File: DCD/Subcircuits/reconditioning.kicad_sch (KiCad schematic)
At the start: 14 parts, among them IC1 830S21AMI-01LF, IC2 830S21AMI-01LF, U15 MC100EP31DTG, U16 MC100EP31DTG, U7 LP2985-33DBVR, U8 CDCLVC1104PWR, Y1 SiT8208AI-21-33E-50.000000

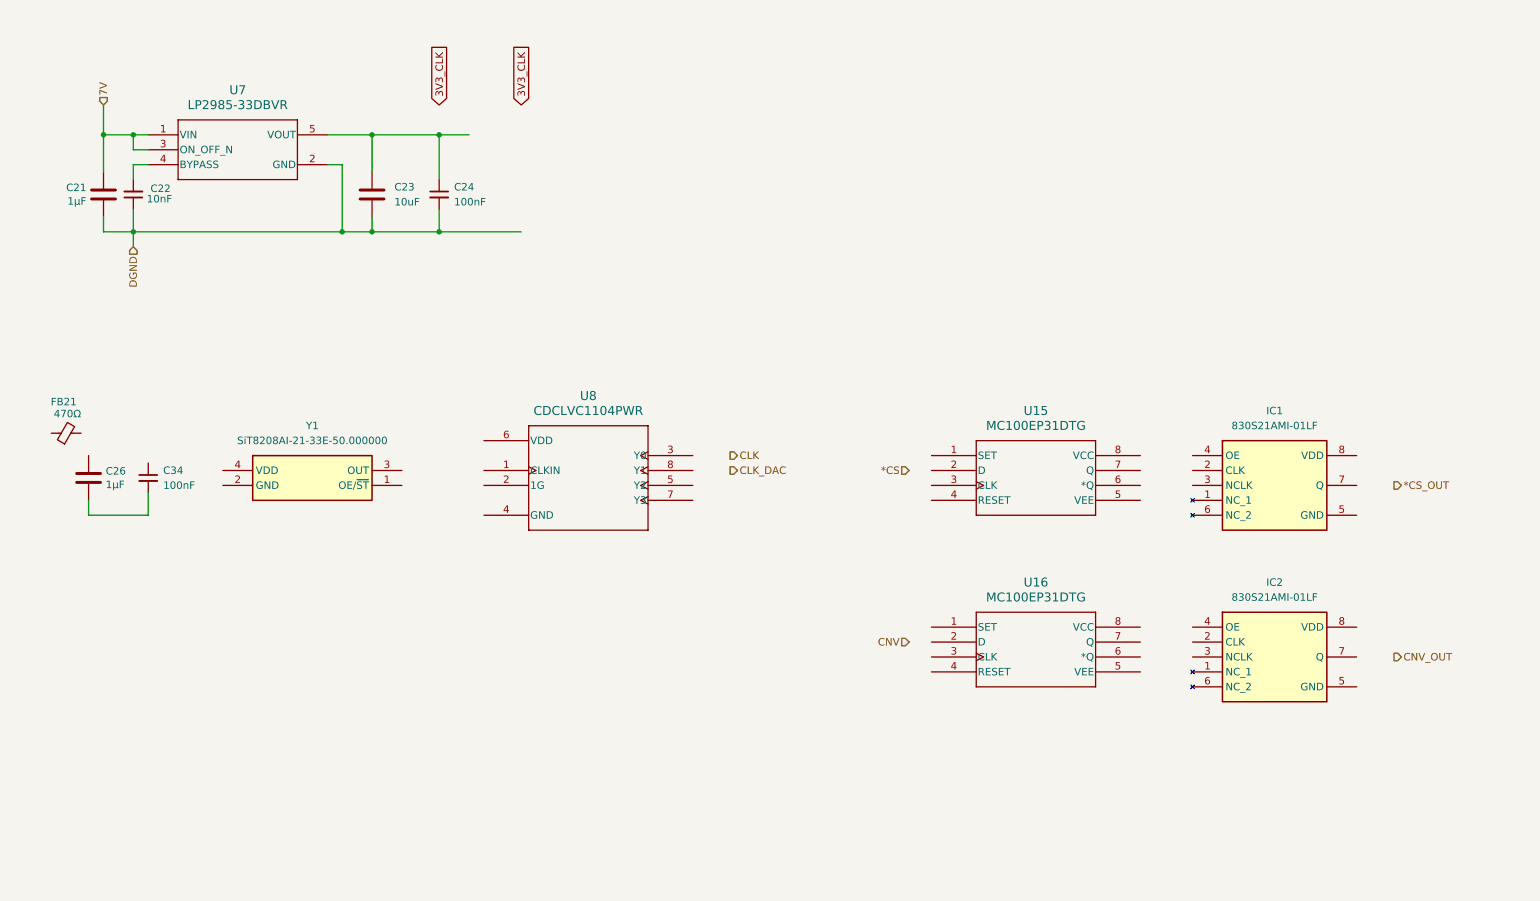
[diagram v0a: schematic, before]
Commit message: Finished the reconditioning circuit
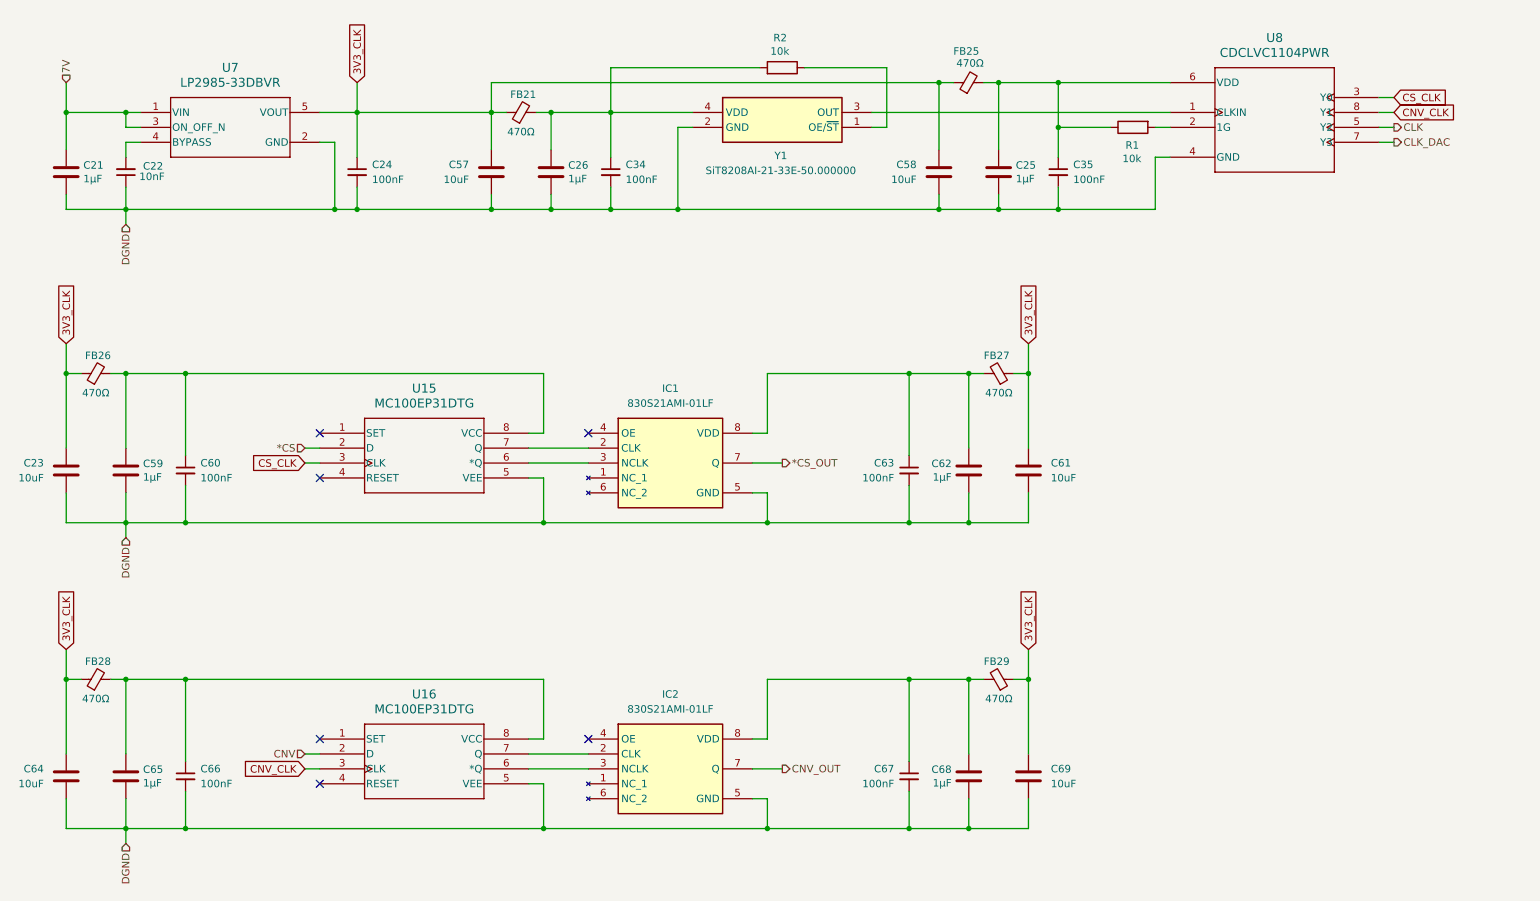
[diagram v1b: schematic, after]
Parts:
- added C25, C59, C62, C65, C68: 1µF, Capacitor_SMD:C_0603_1608Metric, symbol Device:C
- added C35, C60, C63, C66, C67: 100nF, Capacitor_SMD:C_0603_1608Metric, symbol Device:C_Small
- added C57, C58, C61, C64, C69: 10uF, Capacitor_SMD:C_1210_3225Metric, symbol Device:C
- added FB25, FB26, FB27, FB28, FB29: 470Ω, Inductor_SMD:L_0603_1608Metric, symbol Device:FerriteBead_Small
- added R1, R2: 10k, Resistor_SMD:R_0603_1608Metric, symbol Device:R
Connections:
- net *CS: now also U15.2 (D)
- net *CS_OUT: now also IC1.7 (Q)
- net 3V3_CLK: now also C23.1, C24.1, FB21.1, U7.5 (VOUT), C57.1, C58.1, C61.1, C64.1, C69.1, FB25.1, FB26.1, FB27.1, FB28.1, FB29.1
- net CLK: now also U8.5 (Y2)
- net CLK_DAC: now also U8.7 (Y3)
- net CNV: now also U16.2 (D)
- net CNV_OUT: now also IC2.7 (Q)
- net DGND: now also C26.2, C34.2, IC1.5 (GND), IC2.5 (GND), U15.5 (VEE), U16.5 (VEE), U8.4 (GND), Y1.2 (GND), C25.2, C35.2, C57.2, C58.2, C59.2, C60.2, C61.2, C62.2, C63.2, C64.2, C65.2, C66.2, C67.2, C68.2, C69.2
- net at FB21.2: now also C26.1, C34.1, Y1.4 (VDD), R2.2
- net at Y1.1 (OE/~{ST}): now also R2.1
- net at Y1.3 (OUT): now also U8.1 (CLKIN)
- net CNV_CLK: now reaches U16.3 (CLK)
- net CNV_CLK: now also U8.8 (Y1)
- net at U16.6 (*Q): now also IC2.3 (NCLK)
- net at U16.7 (Q): now also IC2.2 (CLK)
- net at U16.8 (VCC): now also C65.1, C66.1, FB28.2
- net at IC2.8 (VDD): now also C67.1, C68.1, FB29.2
- net at U8.2 (1G): now also R1.2
- net CS_CLK: now reaches U8.3 (Y0)
- net CS_CLK: now also U15.3 (CLK)
- net at U8.6 (VDD): now also C25.1, C35.1, FB25.2, R1.1
- net at IC1.2 (CLK): now also U15.7 (Q)
- net at IC1.3 (NCLK): now also U15.6 (*Q)
- net at IC1.8 (VDD): now also C62.1, C63.1, FB27.2
- net at U15.8 (VCC): now also C59.1, C60.1, FB26.2
- no-connect marks 0 -> 6
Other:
- moved on the sheet: C21, C22, C24, C26, C34, FB21, IC1, IC2, U15, U16, U7, U8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

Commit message: Layout mostly done
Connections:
- net CLK: now also U8.8 (Y1); no longer U8.5 (Y2)
- net CLK_DAC: now also U8.5 (Y2); no longer U8.7 (Y3)
- net CNV_CLK: now also U8.3 (Y0); no longer U8.8 (Y1)
- net CS_CLK: now also U8.7 (Y3); no longer U8.3 (Y0)
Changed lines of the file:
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@@
+		)
+	)
+	(global_label "3V3_CLK"
+		(shape input)
+		(at 80.01 29.21 90)
+		(fields_autoplaced yes)
+		(effects
+			(font
+				(size 1.27 1.27)
+			)
+			(justify left)
+		)
+		(property "Intersheetrefs" "${INTERSHEET_REFS}"
+			(at 80.01 18.1815 90)
+			(effects
+				(font
+					(size 1.27 1.27)
+				)
+				(justify left)
+				(hide yes)
+			)
+		)
+	)
+	(global_label "3V3_CLK"
+		(shape input)
+		(at 194.31 125.73 90)
+		(fields_autoplaced yes)
+		(effects
+			(font
+				(size 1.27 1.27)
+			)
+			(justify left)
+		)
+		(property "Intersheetrefs" "${INTERSHEET_REFS}"
+			(at 194.31 114.7015 90)
+			(effects
+				(font
+					(size 1.27 1.27)
+				)
+				(justify left)
+				(hide yes)
+			)
+		)
+	)
+	(global_label "CS_CLK"
+		(shape input)
+		(at 256.54 39.37 0)
+		(fields_autoplaced yes)
+		(effects
+			(font
+				(size 1.27 1.27)
+			)
+			(justify left)
+		)
+		(property "Intersheetrefs" "${INTERSHEET_REFS}"
+			(at 266.5404 39.37 0)
+			(effects
+				(font
+					(size 1.27 1.27)
+				)
+				(justify left)
+				(hide yes)
+			)
+		)
+	)
+	(global_label "3V3_CLK"
+		(shape input)
+		(at 30.48 125.73 90)
+		(fields_autoplaced yes)
+		(effects
+			(font
+				(size 1.27 1.27)
+			)
+			(justify left)
+		)
+		(property "Intersheetrefs" "${INTERSHEET_REFS}"
+			(at 30.48 114.7015 90)
+			(effects
+				(font
+					(size 1.27 1.27)
+				)
+				(justify left)
+				(hide yes)
+			)
 		)
 	)
 	(global_label "CNV_CLK"
 		(shape input)
+		(at 256.54 31.75 0)
+		(fields_autoplaced yes)
+		(effects
+			(font
+				(size 1.27 1.27)
+			)
+			(justify left)
+		)
+		(property "Intersheetrefs" "${INTERSHEET_REFS}"
+			(at 267.75 31.75 0)
+			(effects
+				(font
+					(size 1.27 1.27)
+				)
+				(justify left)
+				(hide yes)
+			)
+		)
+	)
+	(global_label "CNV_CLK"
+		(shape input)
+		(at 71.12 146.05 180)
+		(fields_autoplaced yes)
+		(effects
+			(font
+				(size 1.27 1.27)
+			)
+			(justify right)
+		)
+		(property "Intersheetrefs" "${INTERSHEET_REFS}"
+			(at 59.91 146.05 0)
+			(effects
+				(font
+					(size 1.27 1.27)
+				)
+				(justify right)
+				(hide yes)
+			)
+		)
+	)
+	(hierarchical_label "CLK"
+		(shape output)
 		(at 256.54 34.29 0)
-		(fields_autoplaced yes)
-		(effects
-			(font
-				(size 1.27 1.27)
-			)
-			(justify left)
-		)
-		(property "Intersheetrefs" "${INTERSHEET_REFS}"
-			(at 267.75 34.29 0)
-			(effects
-				(font
-					(size 1.27 1.27)
-				)
-				(justify left)
-				(hide yes)
-			)
-		)
-	)
-	(global_label "3V3_CLK"
-		(shape input)
-		(at 80.01 29.21 90)
-		(fields_autoplaced yes)
-		(effects
-			(font
-				(size 1.27 1.27)
-			)
-			(justify left)
-		)
-		(property "Intersheetrefs" "${INTERSHEET_REFS}"
-			(at 80.01 18.1815 90)
-			(effects
-				(font
-					(size 1.27 1.27)
-				)
-				(justify left)
-				(hide yes)
-			)
-		)
-	)
-	(global_label "3V3_CLK"
-		(shape input)
-		(at 194.31 125.73 90)
-		(fields_autoplaced yes)
-		(effects
-			(font
-				(size 1.27 1.27)
-			)
-			(justify left)
-		)
-		(property "Intersheetrefs" "${INTERSHEET_REFS}"
-			(at 194.31 114.7015 90)
-			(effects
-				(font
-					(size 1.27 1.27)
-				)
-				(justify left)
-				(hide yes)
-			)
-		)
-	)
-	(global_label "CS_CLK"
-		(shape input)
-		(at 256.54 31.75 0)
-		(fields_autoplaced yes)
-		(effects
-			(font
-				(size 1.27 1.27)
-			)
-			(justify left)
-		)
-		(property "Intersheetrefs" "${INTERSHEET_REFS}"
-			(at 266.5404 31.75 0)
-			(effects
-				(font
-					(size 1.27 1.27)
-				)
-				(justify left)
-				(hide yes)
-			)
-		)
-	)
-	(global_label "3V3_CLK"
-		(shape input)
-		(at 30.48 125.73 90)
-		(fields_autoplaced yes)
-		(effects
-			(font
-				(size 1.27 1.27)
-			)
-			(justify left)
-		)
-		(property "Intersheetrefs" "${INTERSHEET_REFS}"
-			(at 30.48 114.7015 90)
-			(effects
-				(font
-					(size 1.27 1.27)
-				)
-				(justify left)
-				(hide yes)
-			)
-		)
-	)
-	(global_label "CNV_CLK"
-		(shape input)
-		(at 71.12 146.05 180)
-		(fields_autoplaced yes)
-		(effects
-			(font
-				(size 1.27 1.27)
-			)
-			(justify right)
-		)
-		(property "Intersheetrefs" "${INTERSHEET_REFS}"
-			(at 59.91 146.05 0)
-			(effects
-				(font
-					(size 1.27 1.27)
-				)
-				(justify right)
-				(hide yes)
-			)
+		(effects
+			(font
+				(size 1.27 1.27)
+			)
+			(justify left)
 		)
 	)
@@
 		)
 	)
+	(hierarchical_label "CLK_DAC"
+		(shape output)
+		(at 256.54 36.83 0)
+		(effects
+			(font
+				(size 1.27 1.27)
+			)
+			(justify left)
+		)
+	)
 	(hierarchical_label "DGND"
 		(shape input)
@@
 		)
 	)
-	(hierarchical_label "CLK_DAC"
-		(shape output)
-		(at 256.54 39.37 0)
-		(effects
-			(font
-				(size 1.27 1.27)
-			)
-			(justify left)
-		)
-	)
 	(hierarchical_label "7V"
 		(shape input)
@@
 		(effects
 			(font
-				(size 1.27 1.27)
-			)
-			(justify left)
-		)
-	)
-	(hierarchical_label "CLK"
-		(shape output)
-		(at 256.54 36.83 0)
-		(effects
-			(font

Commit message: Progrezz
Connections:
- net CLK_DAC: now also U8.7 (Y3); no longer U8.5 (Y2)
- net CS_CLK: now also U8.5 (Y2); no longer U8.7 (Y3)
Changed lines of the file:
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@@
 	(generator_version "9.0")
 	(paper "A4")
+	(text_box "Lenght matching:\n- clk to DAC\n- clks to FLipFlops\n- outputs of FlipFlops (CNV, CS)"
+		(exclude_from_sim no)
+		(at 233.68 80.01 0)
+		(size 45.72 17.78)
+		(margins 0.9525 0.9525 0.9525 0.9525)
+		(stroke
+			(width 0)
+			(type solid)
+		)
+		(fill
+			(type none)
+		)
+		(effects
+			(font
+				(size 1.27 1.27)
+			)
+			(justify left top)
+		)
+	)
 	(junction
 		(at 123.19 34.29)
@@
 	(global_label "CS_CLK"
 		(shape input)
-		(at 256.54 39.37 0)
+		(at 256.54 36.83 0)
 		(fields_autoplaced yes)
 		(effects
@@
 		)
 		(property "Intersheetrefs" "${INTERSHEET_REFS}"
-			(at 266.5404 39.37 0)
+			(at 266.5404 36.83 0)
 			(effects
 				(font
@@
 		)
 	)
-	(hierarchical_label "CLK_DAC"
-		(shape output)
-		(at 256.54 36.83 0)
-		(effects
-			(font
-				(size 1.27 1.27)
-			)
-			(justify left)
-		)
-	)
 	(hierarchical_label "DGND"
 		(shape input)
@@
 		(effects
 			(font
+				(size 1.27 1.27)
+			)
+			(justify left)
+		)
+	)
+	(hierarchical_label "CLK_DAC"
+		(shape output)
+		(at 256.54 39.37 0)
+		(effects
+			(font

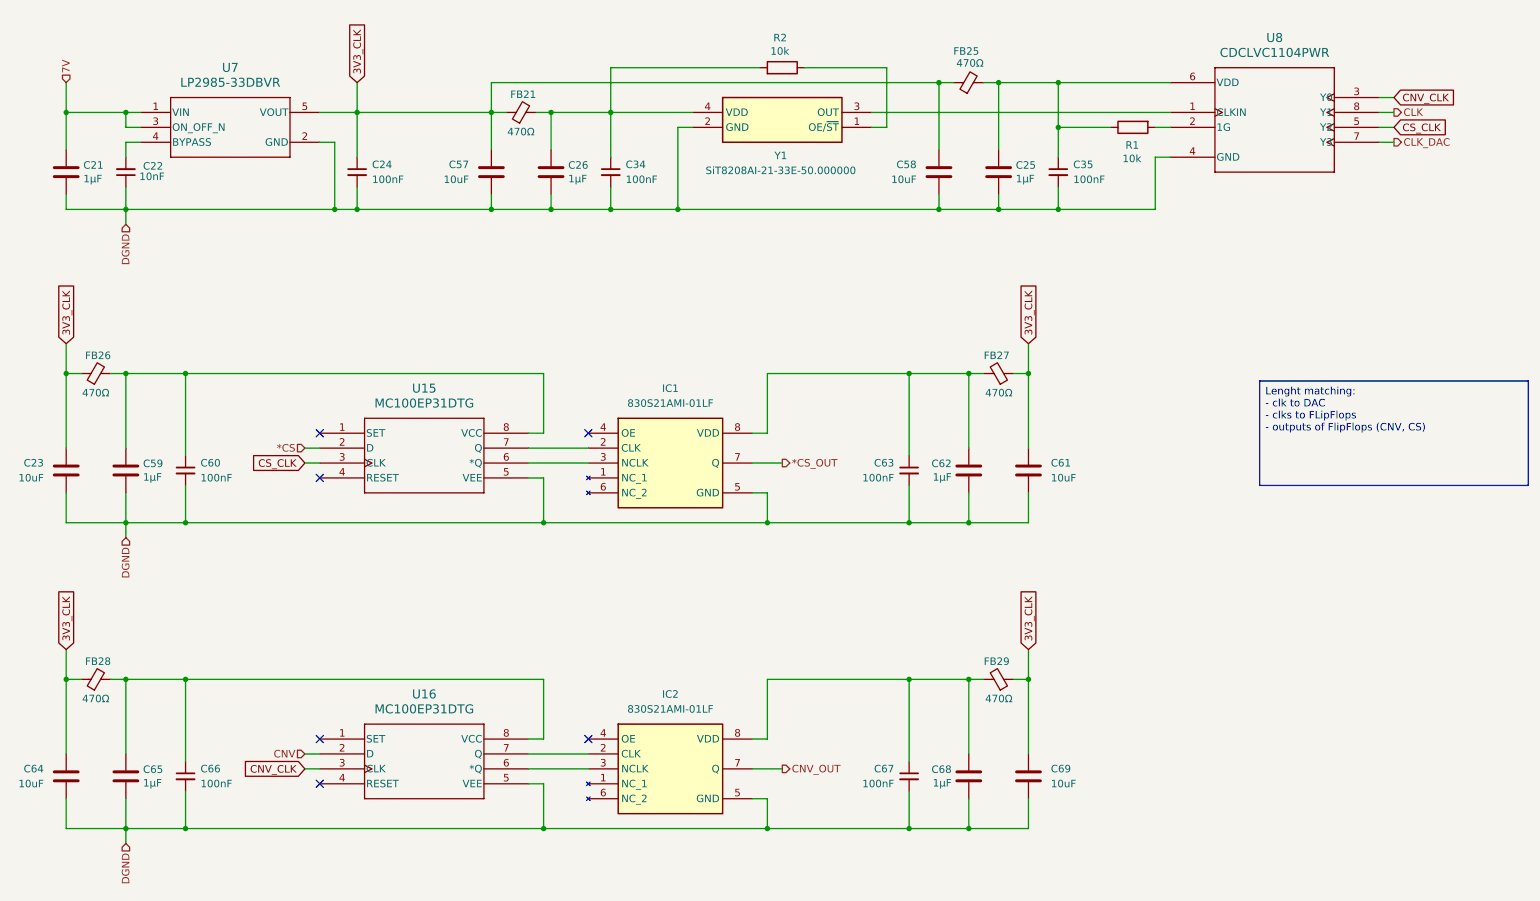
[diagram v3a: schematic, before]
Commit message: Added biasing and termination resistors for the logic gates
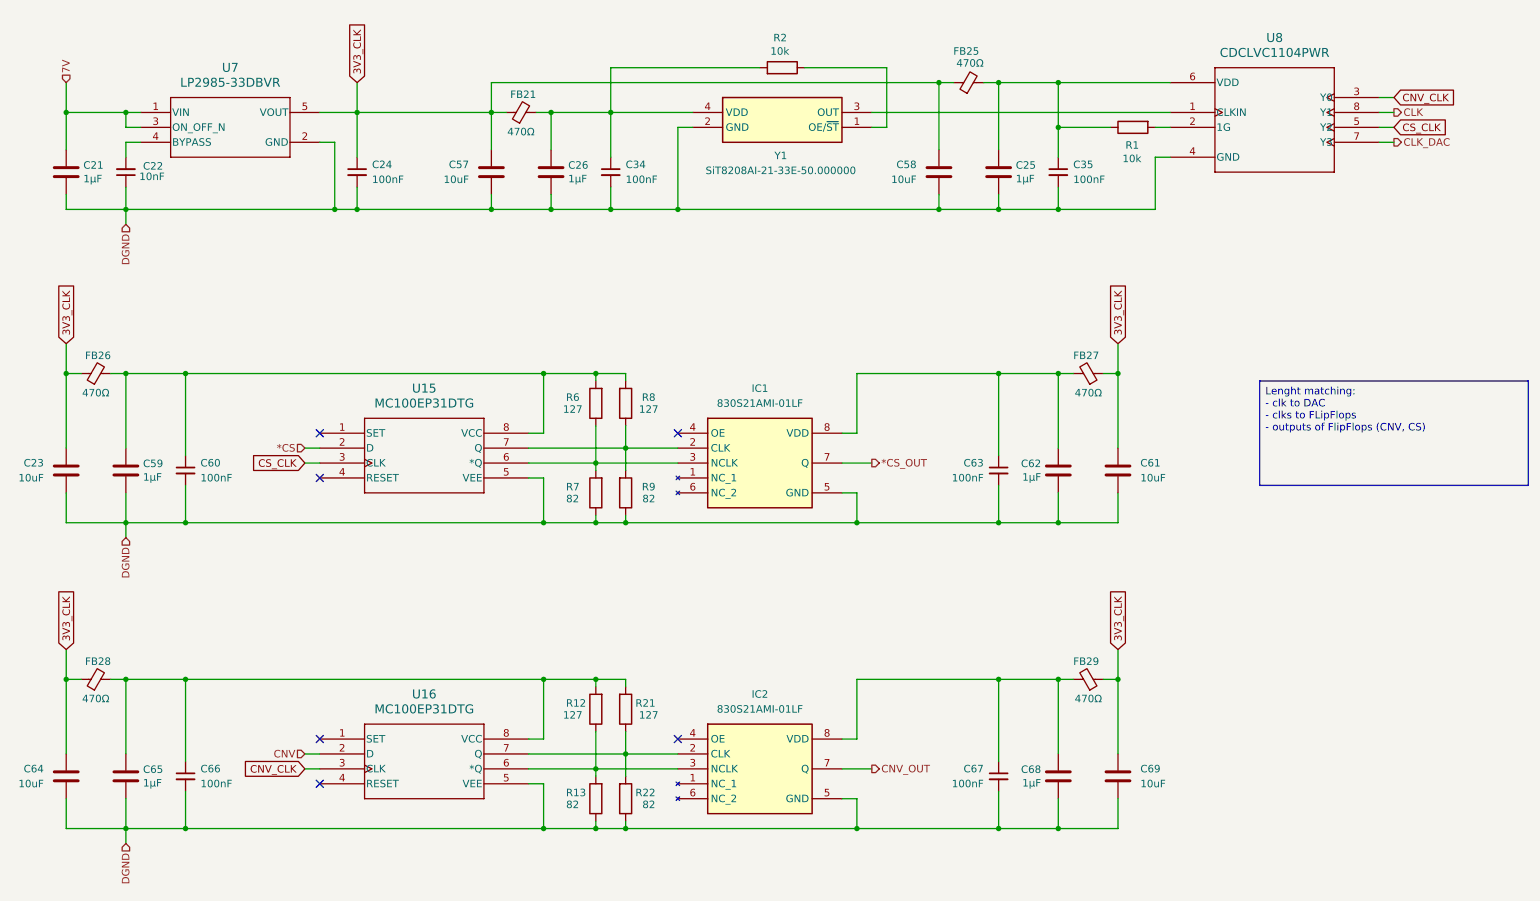
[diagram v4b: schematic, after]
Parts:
- added R12, R21, R6, R8: 127, Resistor_SMD:R_0603_1608Metric, symbol Device:R
- added R13, R22, R7, R9: 82, Resistor_SMD:R_0603_1608Metric, symbol Device:R
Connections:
- net DGND: now also R13.1, R22.1, R7.1, R9.1
- net at C65.1, C66.1, FB28.2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: now also R12.2, R21.2
- net at C59.1, C60.1, FB26.2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: now also R6.2, R8.2
- net at IC2.3 (NCLK), U16.6 (*Q): now also R12.1, R13.2
- net at IC2.2 (CLK), U16.7 (Q): now also R21.1, R22.2
- net at IC1.2 (CLK), U15.7 (Q): now also R8.1, R9.2
- net at IC1.3 (NCLK), U15.6 (*Q): now also R6.1, R7.2
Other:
- moved on the sheet: C61, C62, C63, C67, C68, C69, FB27, FB29, IC1, IC2
